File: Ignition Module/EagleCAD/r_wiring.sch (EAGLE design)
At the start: 52 parts, among them T1 BC848, T2 BC848, T3 BC848, T4 ZXTP2041F, T5 BUB323Z

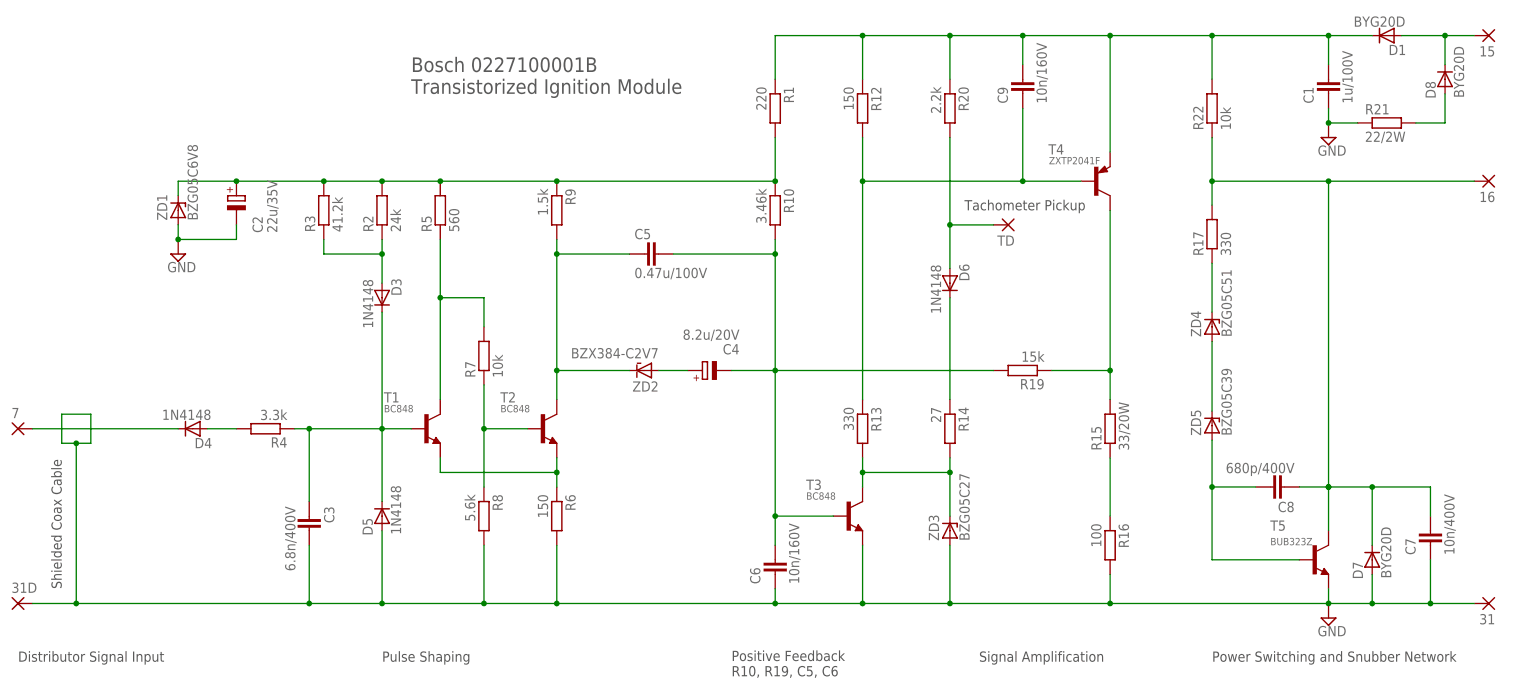
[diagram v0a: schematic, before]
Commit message: Fix missing net
+ Fix missing net T5.B -> R15:R16
+ Rename C8 <-> C9
+ Replace D8 with 1N4148
+ Replace parallel R2 (24k) + R3 (41.2k) with 15.4k R2 only
+ Update PCB layout + routing
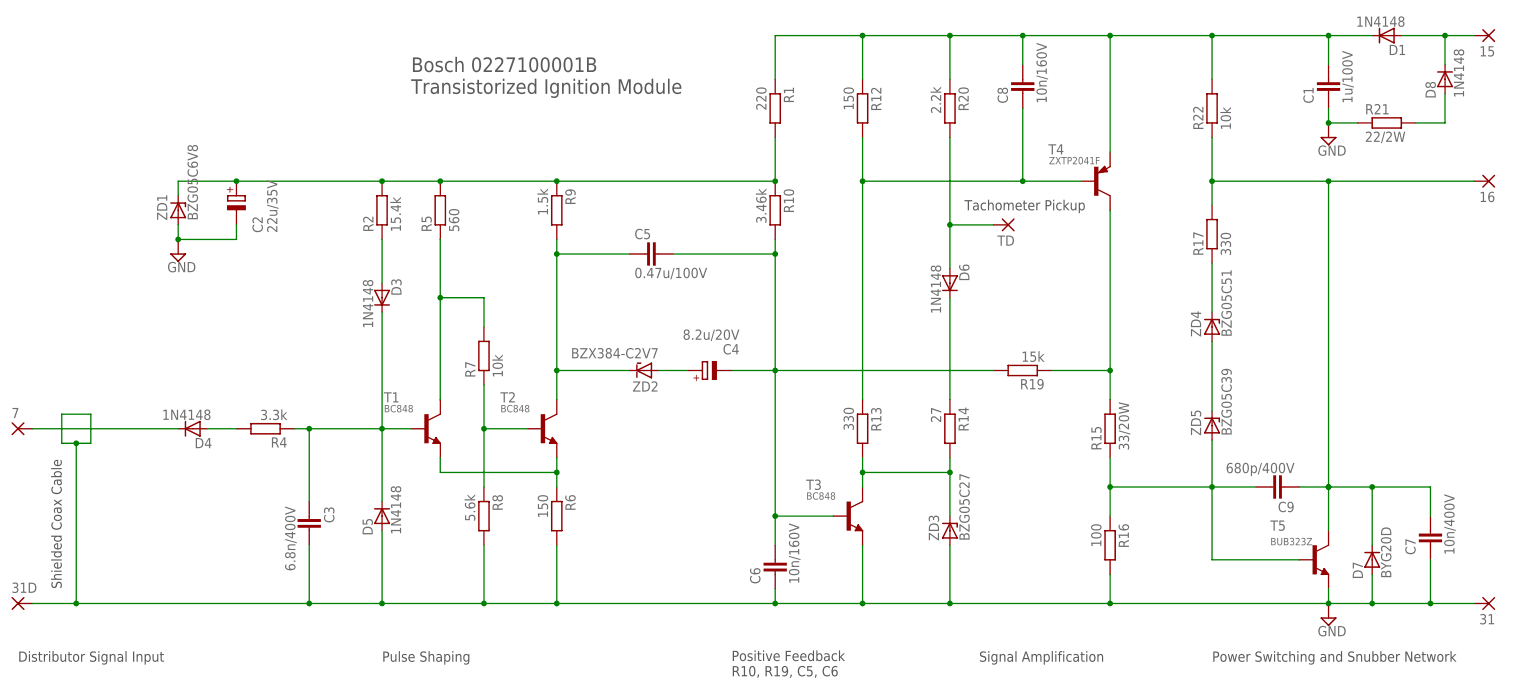
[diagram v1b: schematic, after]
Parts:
- removed R3: 41.2k, resistor:R-EU_R2512
- C8: value 680p/400V -> 10n/160V
- C9: value 10n/160V -> 680p/400V
- D1, D8: value BYG20D -> 1N4148
- R2: value 24k -> 15.4k
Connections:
- removed net N$18: R15.1, R16.1
- net N$10: no longer R3.1
- net N$14: now also C8.1; no longer C9.1
- net N$16: now also C8.2; no longer C9.2
- net N$22: now also C9.2; no longer C8.2
- net N$25: now also C9.1, R15.1, R16.1; no longer C8.1
- net N$8: no longer R3.2
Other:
- moved on the sheet: C8, C9
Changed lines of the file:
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@@
 <?xml version="1.0" encoding="utf-8"?>
 <!DOCTYPE eagle SYSTEM "eagle.dtd">
-<eagle version="7.4.0">
+<eagle version="7.5.0">
 <drawing>
 <settings>
@@
 <part name="C5" library="rcl" deviceset="C-EU" device="C1206" value="0.47u/100V"/>
 <part name="C3" library="rcl" deviceset="C-EU" device="C1206" value="6.8n/400V"/>
-<part name="C8" library="rcl" deviceset="C-EU" device="C1206" value="680p/400V"/>
-<part name="C9" library="rcl" deviceset="C-EU" device="C1206" value="10n/160V"/>
+<part name="C9" library="rcl" deviceset="C-EU" device="C1206" value="680p/400V"/>
+<part name="C8" library="rcl" deviceset="C-EU" device="C1206" value="10n/160V"/>
 <part name="R16" library="rcl" deviceset="R-EU_" device="R2512" value="100"/>
 <part name="R22" library="rcl" deviceset="R-EU_" device="R2512" value="10k"/>
 <part name="R19" library="rcl" deviceset="R-EU_" device="R2512" value="15k"/>
 <part name="T4" library="transistor" deviceset="*-PNP-" device="SOT23-BCE" value="ZXTP2041F"/>
-<part name="D1" library="diode" deviceset="DIODE-" device="SOD123" value="BYG20D"/>
-<part name="D8" library="diode" deviceset="DIODE-" device="SOD123" value="BYG20D"/>
+<part name="D1" library="diode" deviceset="DIODE-" device="SOD123" value="1N4148"/>
+<part name="D8" library="diode" deviceset="DIODE-" device="SOD123" value="1N4148"/>
 <part name="D7" library="diode" deviceset="DIODE-" device="DO214AC" value="BYG20D"/>
 <part name="D6" library="diode" deviceset="DIODE-" device="SOD123" value="1N4148"/>
@@
 <part name="R7" library="resistor" deviceset="R-EU_" device="R2512" value="10k"/>
 <part name="R5" library="resistor" deviceset="R-EU_" device="R2512" value="560"/>
-<part name="R2" library="resistor" deviceset="R-EU_" device="R2512" value="24k"/>
-<part name="R3" library="resistor" deviceset="R-EU_" device="R2512" value="41.2k"/>
+<part name="R2" library="resistor" deviceset="R-EU_" device="R2512" value="15.4k"/>
 <part name="R4" library="resistor" deviceset="R-EU_" device="R2512" value="3.3k"/>
 <part name="R6" library="resistor" deviceset="R-EU_" device="R2512" value="150"/>
@@
 <instance part="C5" gate="G$1" x="76.2" y="55.88" rot="R270"/>
 <instance part="C3" gate="G$1" x="15.24" y="7.62" rot="R180"/>
-<instance part="C8" gate="G$1" x="182.88" y="15.24" rot="R90"/>
-<instance part="C9" gate="G$1" x="139.7" y="86.36"/>
+<instance part="C9" gate="G$1" x="182.88" y="15.24" rot="R90"/>
+<instance part="C8" gate="G$1" x="139.7" y="86.36"/>
 <instance part="R16" gate="G$1" x="154.94" y="5.08" rot="R270"/>
 <instance part="R22" gate="G$1" x="172.72" y="81.28" rot="R90"/>
@@
 <instance part="R5" gate="G$1" x="38.1" y="63.5" rot="R90"/>
 <instance part="R2" gate="G$1" x="27.94" y="63.5" rot="R90"/>
-<instance part="R3" gate="G$1" x="17.78" y="63.5" rot="R90"/>
 <instance part="R4" gate="G$1" x="7.62" y="25.4" rot="R180"/>
 <instance part="R6" gate="G$1" x="58.42" y="10.16" rot="R270"/>
@@
 <pinref part="C2" gate="G$1" pin="+"/>
 <wire x1="-7.62" y1="68.58" x2="2.54" y2="68.58" width="0.1524" layer="91"/>
-<pinref part="R3" gate="G$1" pin="2"/>
-<wire x1="2.54" y1="68.58" x2="17.78" y2="68.58" width="0.1524" layer="91"/>
+<wire x1="2.54" y1="68.58" x2="27.94" y2="68.58" width="0.1524" layer="91"/>
 <pinref part="R2" gate="G$1" pin="2"/>
-<wire x1="17.78" y1="68.58" x2="27.94" y2="68.58" width="0.1524" layer="91"/>
 <pinref part="R5" gate="G$1" pin="2"/>
 <wire x1="27.94" y1="68.58" x2="38.1" y2="68.58" width="0.1524" layer="91"/>
@@
 <wire x1="38.1" y1="68.58" x2="58.42" y2="68.58" width="0.1524" layer="91"/>
 <junction x="2.54" y="68.58"/>
-<junction x="17.78" y="68.58"/>
 <junction x="27.94" y="68.58"/>
 <junction x="38.1" y="68.58"/>
@@
 <net name="N$10" class="0">
 <segment>
-<pinref part="R3" gate="G$1" pin="1"/>
-<wire x1="17.78" y1="58.42" x2="17.78" y2="55.88" width="0.1524" layer="91"/>
-<wire x1="17.78" y1="55.88" x2="27.94" y2="55.88" width="0.1524" layer="91"/>
 <pinref part="R2" gate="G$1" pin="1"/>
-<wire x1="27.94" y1="55.88" x2="27.94" y2="58.42" width="0.1524" layer="91"/>
 <pinref part="D3" gate="G$1" pin="A"/>
-<wire x1="27.94" y1="55.88" x2="27.94" y2="50.8" width="0.1524" layer="91"/>
-<junction x="27.94" y="55.88"/>
+<wire x1="27.94" y1="58.42" x2="27.94" y2="50.8" width="0.1524" layer="91"/>
 </segment>
 </net>
@@
 <pinref part="T4" gate="G$1" pin="B"/>
 <wire x1="111.76" y1="68.58" x2="139.7" y2="68.58" width="0.1524" layer="91"/>
-<pinref part="C9" gate="G$1" pin="2"/>
+<pinref part="C8" gate="G$1" pin="2"/>
 <wire x1="139.7" y1="68.58" x2="149.86" y2="68.58" width="0.1524" layer="91"/>
 <wire x1="139.7" y1="81.28" x2="139.7" y2="68.58" width="0.1524" layer="91"/>
@@
 <pinref part="R20" gate="G$1" pin="1"/>
 <wire x1="127" y1="86.36" x2="127" y2="93.98" width="0.1524" layer="91"/>
-<pinref part="C9" gate="G$1" pin="1"/>
+<pinref part="C8" gate="G$1" pin="1"/>
 <wire x1="139.7" y1="88.9" x2="139.7" y2="93.98" width="0.1524" layer="91"/>
 <junction x="139.7" y="93.98"/>
@@
 </segment>
 </net>
-<net name="N$18" class="0">
-<segment>
-<pinref part="R15" gate="G$1" pin="1"/>
-<pinref part="R16" gate="G$1" pin="1"/>
-<wire x1="154.94" y1="20.32" x2="154.94" y2="10.16" width="0.1524" layer="91"/>
-</segment>
-</net>
 <net name="N$19" class="1">
 <segment>
@@
 <wire x1="193.04" y1="68.58" x2="218.44" y2="68.58" width="0.1524" layer="91"/>
 <wire x1="172.72" y1="68.58" x2="172.72" y2="64.42654375" width="0.1524" layer="91"/>
-<pinref part="C8" gate="G$1" pin="2"/>
+<pinref part="C9" gate="G$1" pin="2"/>
 <pinref part="C7" gate="G$1" pin="1"/>
 <wire x1="187.96" y1="15.24" x2="193.04" y2="15.24" width="0.1524" layer="91"/>
@@
 <pinref part="ZD5" gate="G$1" pin="A"/>
 <wire x1="172.72" y1="23.415928125" x2="172.72" y2="15.24" width="0.1524" layer="91"/>
-<pinref part="C8" gate="G$1" pin="1"/>
+<pinref part="C9" gate="G$1" pin="1"/>
 <wire x1="172.72" y1="15.24" x2="180.34" y2="15.24" width="0.1524" layer="91"/>
 <wire x1="172.72" y1="15.24" x2="172.72" y2="2.54" width="0.1524" layer="91"/>
@@
 <wire x1="172.72" y1="2.54" x2="187.96" y2="2.54" width="0.1524" layer="91"/>
 <junction x="172.72" y="15.24"/>
-</segment>
-</net>
+<pinref part="R15" gate="G$1" pin="1"/>
+<pinref part="R16" gate="G$1" pin="1"/>
+<wire x1="154.94" y1="20.32" x2="154.94" y2="15.24" width="0.1524" layer="91"/>
+<wire x1="154.94" y1="15.24" x2="154.94" y2="10.16" width="0.1524" layer="91"/>
+<wire x1="172.72" y1="15.24" x2="154.94" y2="15.24" width="0.1524" layer="91"/>
+<junction x="154.94" y="15.24"/>
+</segment>
+</net>
